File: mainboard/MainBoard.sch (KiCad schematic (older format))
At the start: 51 parts, among them J1 isoSPI, J11 ON_HANDCART, J3 IMD, J4 IO, U1 LTC6820, U10 REF2920, U2 HM2103, U3 M24M02, U4 M24M02, U5 STM32F334K8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

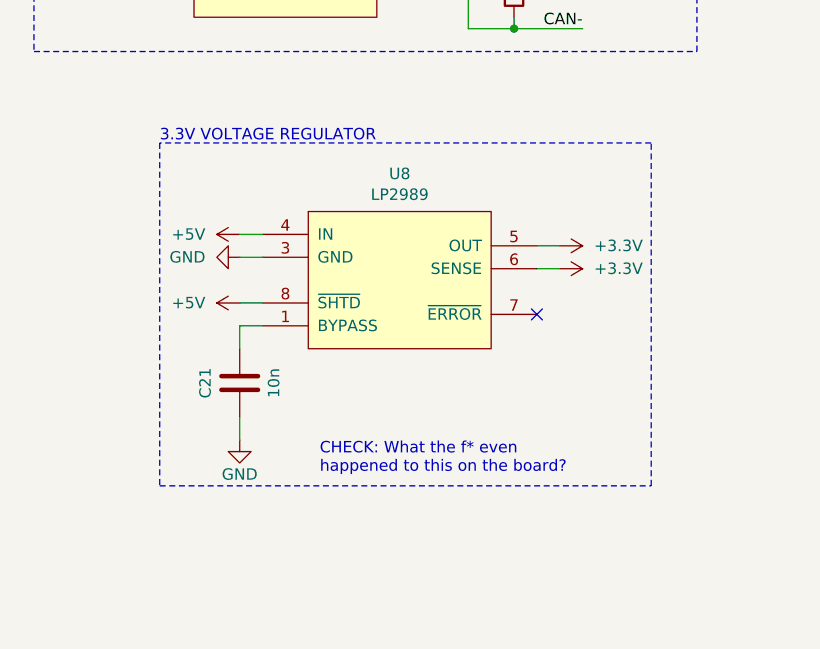
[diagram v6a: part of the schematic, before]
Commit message: Using standard LM1117 regulator
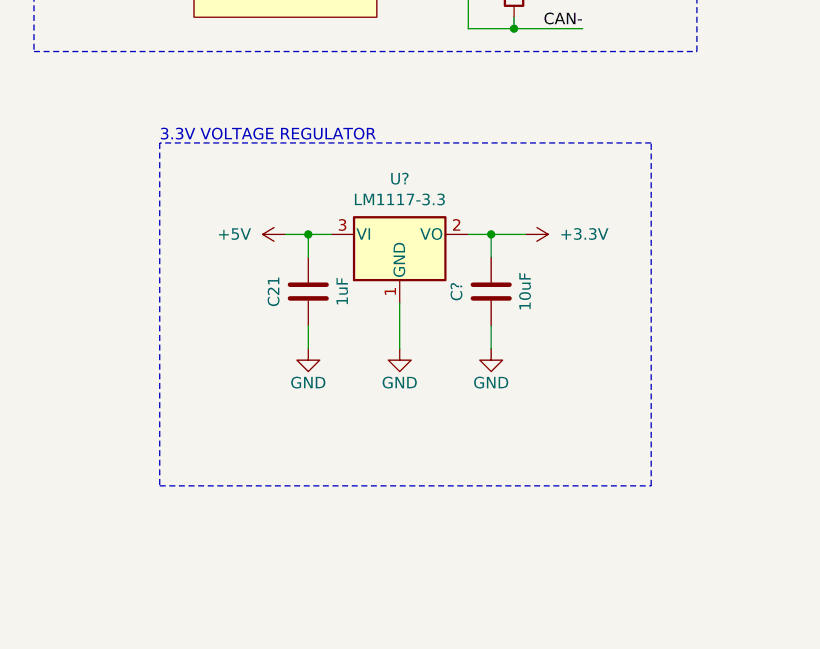
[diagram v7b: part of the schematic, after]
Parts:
- removed U8: LP2989, MainBoard:SOIC-8, symbol MainBoard:LP2989
- added C?: 10uF, Capacitor_SMD:C_0805_2012Metric, symbol Device:C
- added U?: LM1117-3.3, symbol Regulator_Linear:LM1117-3.3
- C21: value 10n -> 1uF
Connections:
- net +3V3: now also C?.1, U?.2 (VO)
- net +5V: now also C21.1, U?.3 (VI)
- net GND: now also C?.2, U?.1 (GND)
- no-connect marks 11 -> 10
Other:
- note removed: "CHECK: What the f* even \nhappened to this on the board?"
- moved on the sheet: C21
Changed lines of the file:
@@
 Wire Wire Line
 	3100 550  3500 550
-Wire Wire Line
-	9700 5450 9800 5450
-Wire Wire Line
-	9700 5350 9800 5350
-Wire Wire Line
-	8500 5300 8400 5300
-Wire Wire Line
-	8500 5400 8400 5400
 $Comp
 L power:+5V #PWR045
 U 1 1 5AF3CCEF
-P 8400 5300
-F 0 "#PWR045" H 8400 5150 50  0001 C CNN
-F 1 "+5V" V 8400 5450 50  0000 L CNN
-F 2 "" H 8400 5300 50  0001 C CNN
-F 3 "" H 8400 5300 50  0001 C CNN
-	1    8400 5300
+P 8600 5300
+F 0 "#PWR045" H 8600 5150 50  0001 C CNN
+F 1 "+5V" V 8600 5450 50  0000 L CNN
+F 2 "" H 8600 5300 50  0001 C CNN
+F 3 "" H 8600 5300 50  0001 C CNN
+	1    8600 5300
 	0    -1   -1   0
 $EndComp
@@
 L power:GND #PWR047
 U 1 1 5AF3CE80
-P 8400 5400
-F 0 "#PWR047" H 8400 5150 50  0001 C CNN
-F 1 "GND" V 8400 5250 50  0000 R CNN
-F 2 "" H 8400 5400 50  0001 C CNN
-F 3 "" H 8400 5400 50  0001 C CNN
-	1    8400 5400
-	0    1    1    0
-$EndComp
-$Comp
-L power:+3.3V #PWR046
-U 1 1 5AF3CEC7
-P 9800 5350
-F 0 "#PWR046" H 9800 5200 50  0001 C CNN
-F 1 "+3.3V" V 9800 5500 50  0000 L CNN
-F 2 "" H 9800 5350 50  0001 C CNN
-F 3 "" H 9800 5350 50  0001 C CNN
-	1    9800 5350
-	0    1    1    0
-$EndComp
-$Comp
-L power:+3.3V #PWR048
-U 1 1 5AF3CF2C
-P 9800 5450
-F 0 "#PWR048" H 9800 5300 50  0001 C CNN
-F 1 "+3.3V" V 9800 5600 50  0000 L CNN
-F 2 "" H 9800 5450 50  0001 C CNN
-F 3 "" H 9800 5450 50  0001 C CNN
-	1    9800 5450
-	0    1    1    0
-$EndComp
-Wire Wire Line
-	8500 5600 8400 5600
-$Comp
-L power:+5V #PWR049
-U 1 1 5AF44955
-P 8400 5600
-F 0 "#PWR049" H 8400 5450 50  0001 C CNN
-F 1 "+5V" V 8400 5750 50  0000 L CNN
-F 2 "" H 8400 5600 50  0001 C CNN
-F 3 "" H 8400 5600 50  0001 C CNN
-	1    8400 5600
-	0    -1   -1   0
-$EndComp
-Wire Wire Line
-	8500 5700 8400 5700
-Wire Wire Line
-	8400 5700 8400 5800
+P 9100 5800
+F 0 "#PWR047" H 9100 5550 50  0001 C CNN
+F 1 "GND" H 9100 5650 50  0000 C CNN
+F 2 "" H 9100 5800 50  0001 C CNN
+F 3 "" H 9100 5800 50  0001 C CNN
+	1    9100 5800
+	1    0    0    -1
+$EndComp
 $Comp
 L Device:C C21
 U 1 1 5AF4C54C
-P 8400 5950
-F 0 "C21" V 8250 5950 50  0000 C CNN
-F 1 "10n" V 8550 5950 50  0000 C CNN
-F 2 "Capacitor_SMD:C_0805_2012Metric" H 8438 5800 50  0001 C CNN
-F 3 "~" H 8400 5950 50  0001 C CNN
-	1    8400 5950
-	1    0    0    -1
-$EndComp
-Wire Wire Line
-	8400 6100 8400 6200
+P 8700 5550
+F 0 "C21" V 8550 5550 50  0000 C CNN
+F 1 "1uF" V 8850 5550 50  0000 C CNN
+F 2 "Capacitor_SMD:C_0805_2012Metric" H 8738 5400 50  0001 C CNN
+F 3 "~" H 8700 5550 50  0001 C CNN
+	1    8700 5550
+	1    0    0    -1
+$EndComp
+Wire Wire Line
+	8700 5700 8700 5800
 $Comp
 L power:GND #PWR051
 U 1 1 5AF543CA
-P 8400 6200
-F 0 "#PWR051" H 8400 5950 50  0001 C CNN
-F 1 "GND" H 8400 6050 50  0000 C CNN
-F 2 "" H 8400 6200 50  0001 C CNN
-F 3 "" H 8400 6200 50  0001 C CNN
-	1    8400 6200
-	1    0    0    -1
-$EndComp
-NoConn ~ 9700 5650
-$Comp
-L MainBoard:LP2989 U8
-U 1 1 5AF104C7
-P 9100 5500
-F 0 "U8" H 9100 5965 50  0000 C CNN
-F 1 "LP2989" H 9100 5874 50  0000 C CNN
-F 2 "MainBoard:SOIC-8" H 9100 5150 50  0001 C CNN
-F 3 "http://www.ti.com/lit/ds/symlink/lp2989.pdf" H 9100 5500 50  0001 C CNN
-	1    9100 5500
+P 8700 5800
+F 0 "#PWR051" H 8700 5550 50  0001 C CNN
+F 1 "GND" H 8700 5650 50  0000 C CNN
+F 2 "" H 8700 5800 50  0001 C CNN
+F 3 "" H 8700 5800 50  0001 C CNN
+	1    8700 5800
 	1    0    0    -1
 $EndComp
@@
 Text Notes 600  4200 0    50   ~ 0
 CHECK: unpopulated
-Text Notes 8750 6350 0    50   ~ 0
-CHECK: What the f* even \nhappened to this on the board?
 $Comp
 L Connector_Generic:Conn_02x05_Odd_Even J?
@@
 Wire Notes Line
 	8350 2400 8350 3200
+$Comp
+L Regulator_Linear:LM1117-3.3 U?
+U 1 1 608FC0D4
+P 9100 5300
+F 0 "U?" H 9100 5542 50  0000 C CNN
+F 1 "LM1117-3.3" H 9100 5451 50  0000 C CNN
+F 2 "" H 9100 5300 50  0001 C CNN
+F 3 "http://www.ti.com/lit/ds/symlink/lm1117.pdf" H 9100 5300 50  0001 C CNN
+	1    9100 5300
+	1    0    0    -1
+$EndComp
+Wire Wire Line
+	8700 5400 8700 5300
+Connection ~ 8700 5300
+$Comp
+L Device:C C?
+U 1 1 60989FBB
+P 9500 5550
+F 0 "C?" V 9350 5550 50  0000 C CNN
+F 1 "10uF" V 9650 5550 50  0000 C CNN
+F 2 "Capacitor_SMD:C_0805_2012Metric" H 9538 5400 50  0001 C CNN
+F 3 "~" H 9500 5550 50  0001 C CNN
+	1    9500 5550
+	1    0    0    -1
+$EndComp
+$Comp
+L power:+3.3V #PWR046
+U 1 1 5AF3CEC7
+P 9650 5300
+F 0 "#PWR046" H 9650 5150 50  0001 C CNN
+F 1 "+3.3V" V 9650 5450 50  0000 L CNN
+F 2 "" H 9650 5300 50  0001 C CNN
+F 3 "" H 9650 5300 50  0001 C CNN
+	1    9650 5300
+	0    1    1    0
+$EndComp
+Wire Wire Line
+	8700 5300 8800 5300
+Wire Wire Line
+	8600 5300 8700 5300
+Wire Wire Line
+	9400 5300 9500 5300
+Wire Wire Line
+	9500 5400 9500 5300
+Connection ~ 9500 5300
+Wire Wire Line
+	9500 5300 9650 5300
+$Comp
+L power:GND #PWR?
+U 1 1 60A549B3
+P 9500 5800
+F 0 "#PWR?" H 9500 5550 50  0001 C CNN
+F 1 "GND" H 9500 5650 50  0000 C CNN
+F 2 "" H 9500 5800 50  0001 C CNN
+F 3 "" H 9500 5800 50  0001 C CNN
+	1    9500 5800
+	1    0    0    -1
+$EndComp
+Wire Wire Line
+	9100 5600 9100 5800
+Wire Wire Line
+	9500 5700 9500 5800
 $EndSCHEMATC
